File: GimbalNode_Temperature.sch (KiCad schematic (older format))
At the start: 18 parts

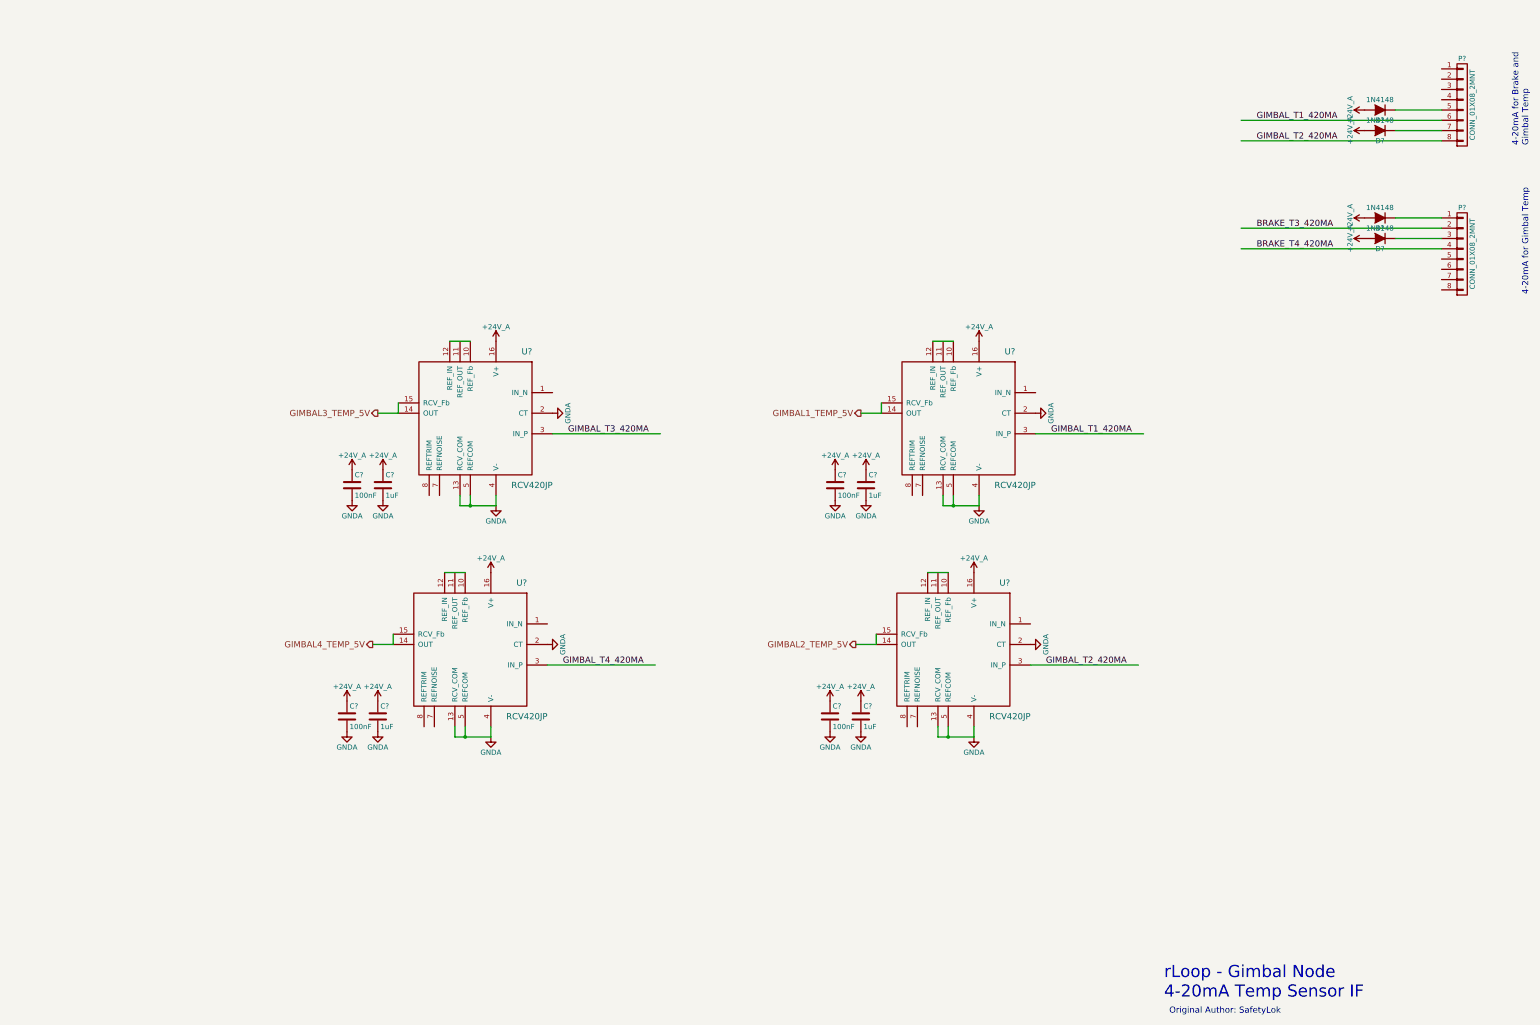
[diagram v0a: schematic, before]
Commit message: Fixup various caps on 4-20ma sheet.
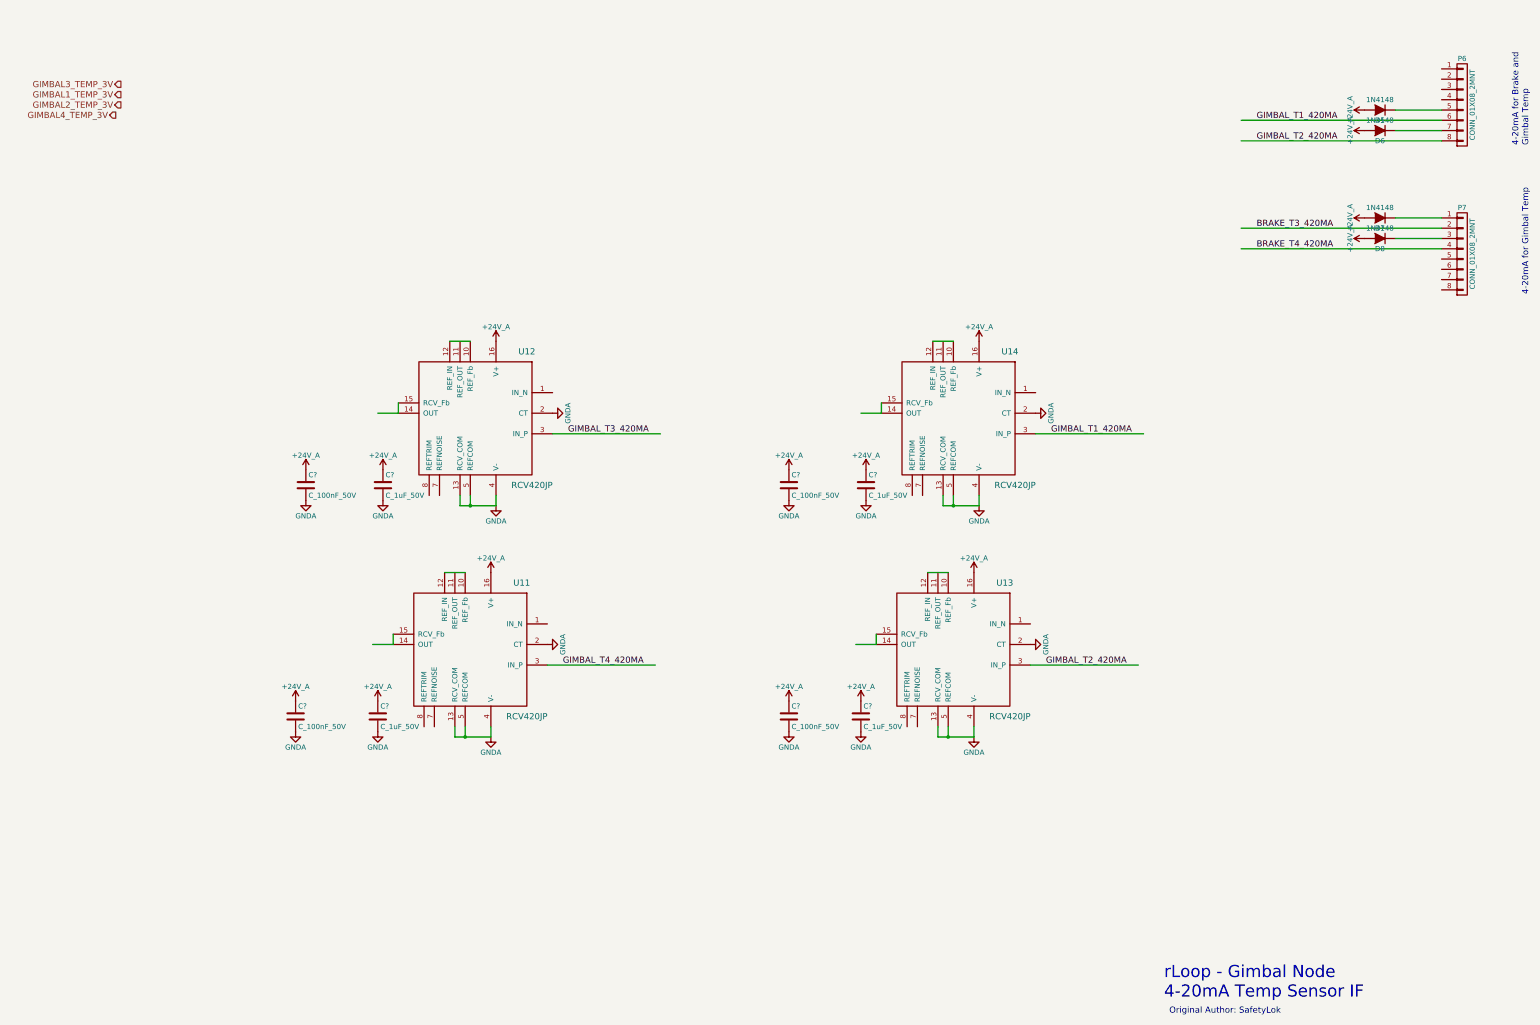
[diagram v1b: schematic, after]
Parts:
- removed C? (x4): 100nF, symbol C
- removed C? (x4): 1uF, symbol C
- added C? (x4): C_100nF_50V, RLOOP_FOOTPRINTS:rLoop_C_0603, symbol C_100nF_50V
- added C? (x4): C_1uF_50V, RLOOP_FOOTPRINTS:rLoop_C_0603, symbol C_1uF_50V
- gave numbers to parts that had none: 10
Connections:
- net labels added: GIMBAL1_TEMP_3V, GIMBAL2_TEMP_3V, GIMBAL3_TEMP_3V, GIMBAL4_TEMP_3V
- net labels removed: GIMBAL1_TEMP_5V, GIMBAL2_TEMP_5V, GIMBAL3_TEMP_5V, GIMBAL4_TEMP_5V

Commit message: Fixup 5V to 3V connections
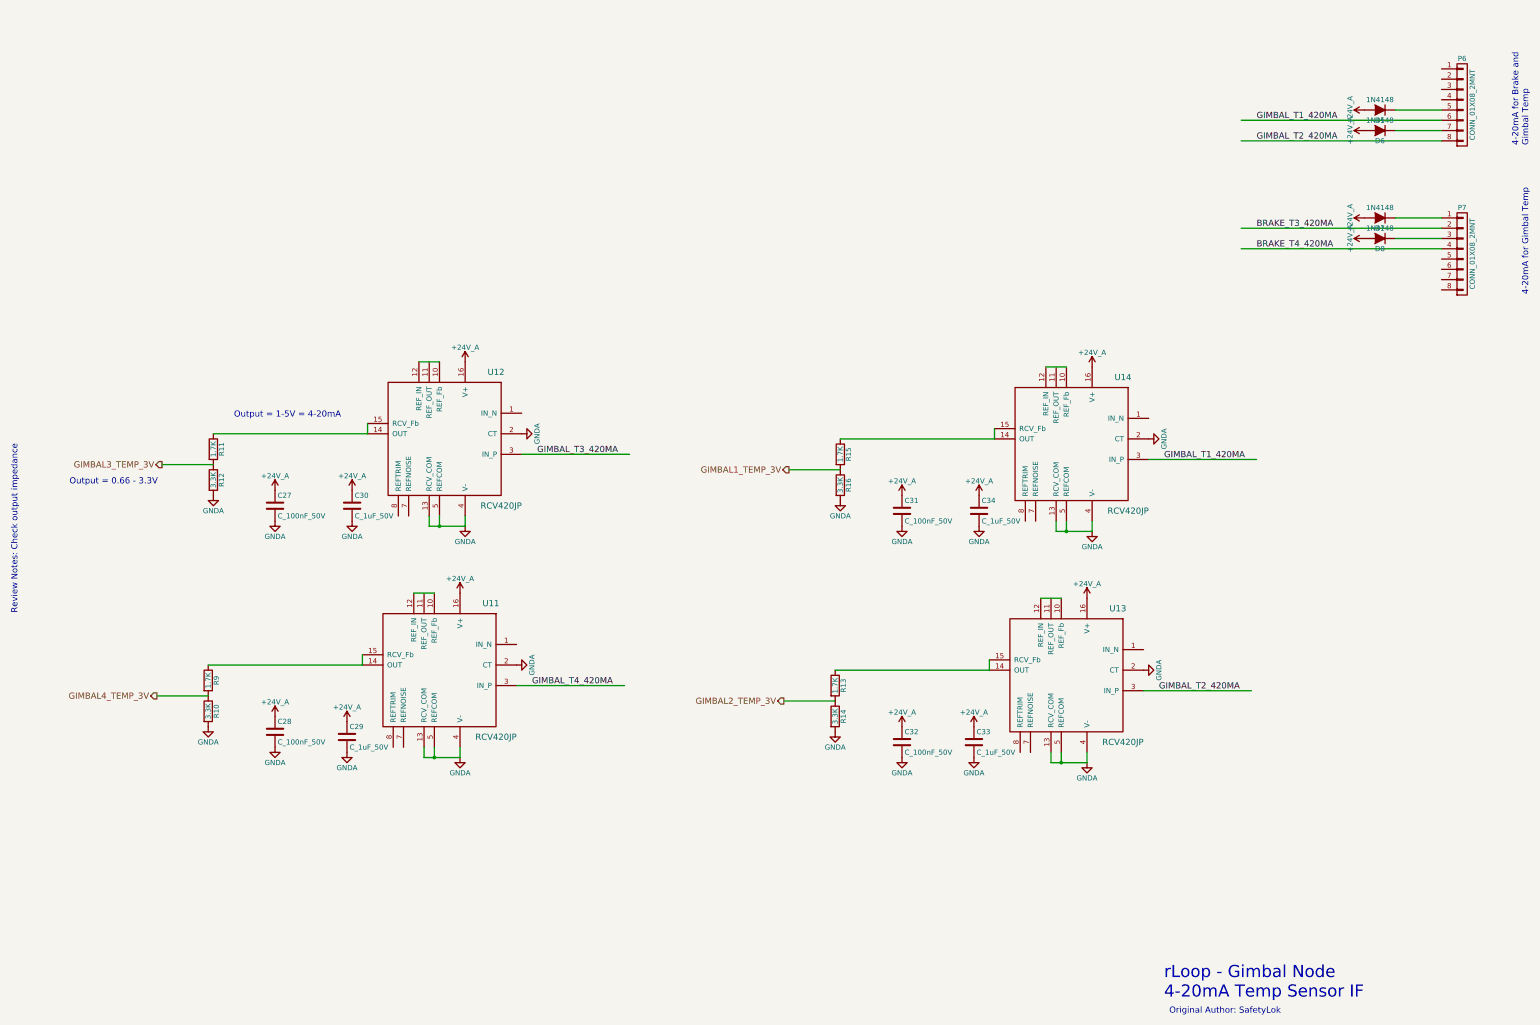
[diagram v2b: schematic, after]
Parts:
- added R10, R12, R14, R16: 3.3K, RLOOP_FOOTPRINTS:rLoop_R_0603, symbol 3.3K
- added R11, R13, R15, R9: 1.7K, RLOOP_FOOTPRINTS:rLoop_R_0603, symbol 1.7K
- gave numbers to parts that had none: 8
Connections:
- wire segments 40 -> 44
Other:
- note added: "Output = 0.66 - 3.3V"
- note added: "Output = 1-5V = 4-20mA"
- note added: "Review Notes: Check output impedance"
- moved on the sheet: C27, C28, C29, C30, C31, C32, C33, C34, U11, U12, U13, U14

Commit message: Update connectors, diodes, add zener's and anotate.
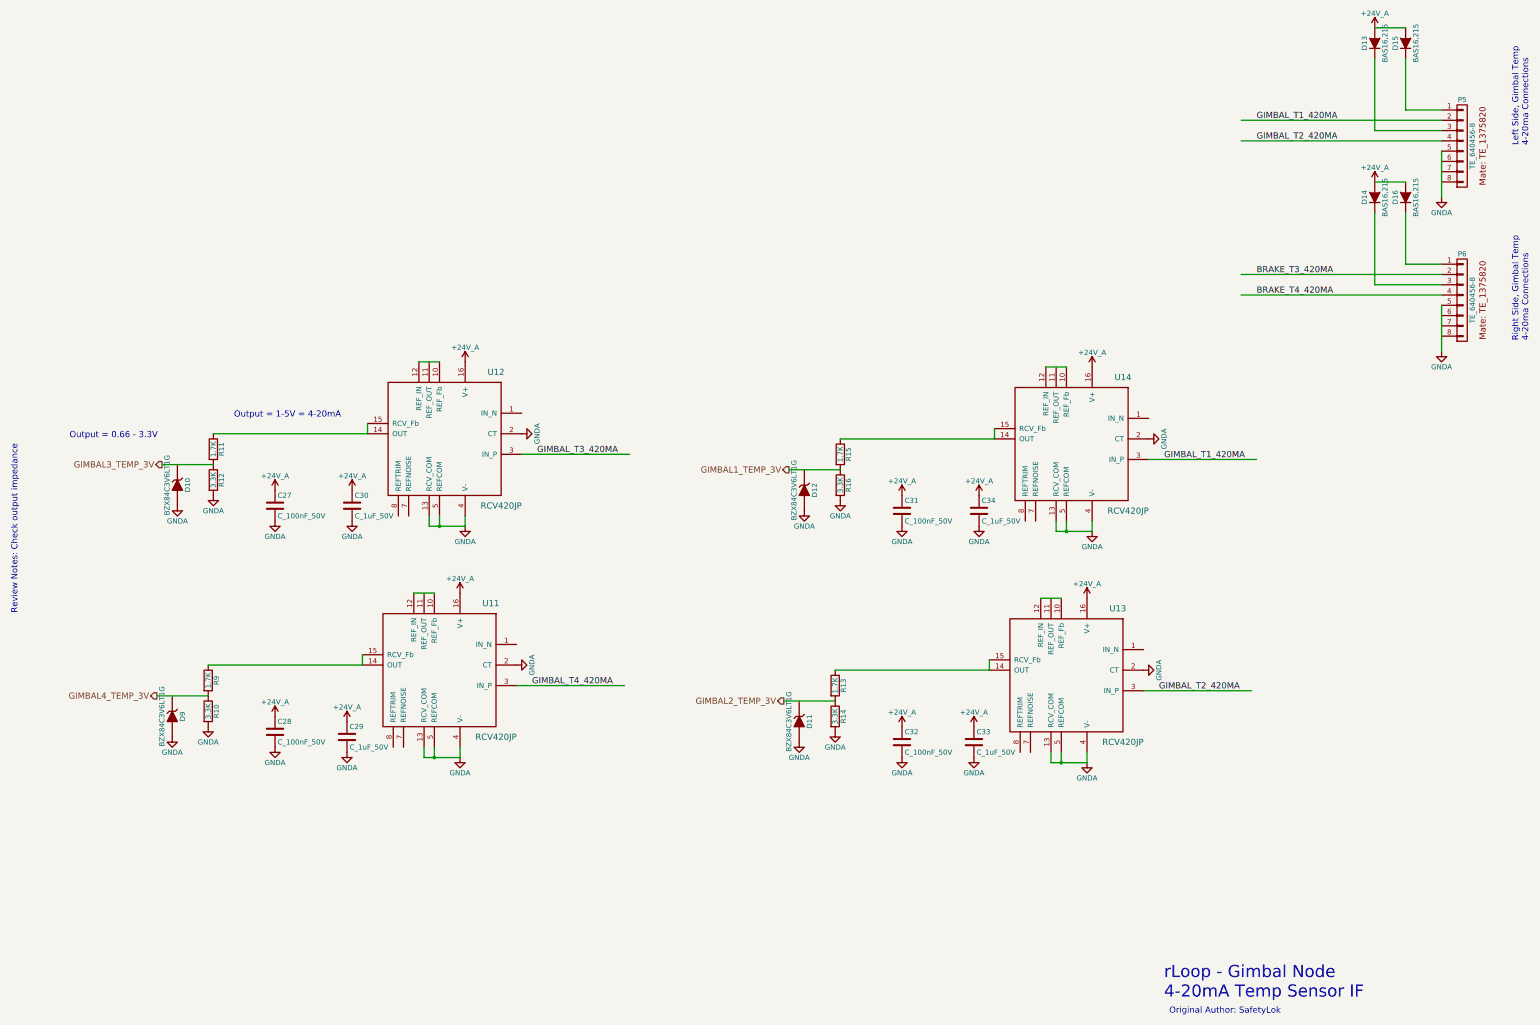
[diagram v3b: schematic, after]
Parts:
- removed D5, D6, D7, D8: 1N4148, symbol D
- removed P6, P7: CONN_01X08_2MNT, symbol CONN_01X08_2MNT
- added D10, D11, D12, D9: BZX84C3V6LT1G, RLOOP_FOOTPRINTS:rLoop_SOT23, symbol BZX84C3V6LT1G
- added D13, D14, D15, D16: BAS16,215, RLOOP_FOOTPRINTS:rLoop_SOT23, symbol BAS16,215
- added P5, P6: TE_640456-8, RLOOP_FOOTPRINTS:rLoop_TE640456-8, symbol TE_640456-8
- U11, U12, U13, U14: footprint (none) -> RLOOP_FOOTPRINTS:rLoop_DIP16
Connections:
- wire segments 44 -> 52
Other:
- note added: "Left Side, Gimbal Temp\n4-20ma Connections"
- note added: "Right Side, Gimbal Temp\n4-20ma Connections"
- note removed: "4-20mA for Brake and\nGimbal Temp"
- note removed: "4-20mA for Gimbal Temp"
